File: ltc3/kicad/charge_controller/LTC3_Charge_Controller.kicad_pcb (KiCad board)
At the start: 4 copper layers, 85.2 x 81.3 mm, 119 parts, among them P1 MicroFit header, P2 MicroFit header, P3 S2BPHKS, P4 MicroFit header, P5 JST XH header, P7 JST XH header, Q1 ZVN4525E6, Q2 BSC028N06NS, Q3 BSC028N06NS, Q4 BSC028N06NS, Q5 BSC028N06NS, Q6 ZVP3310F, Q7 MMBT5550L, U1 PI2127, U2 PI2127, U3 LT8490, U4 LTC2990

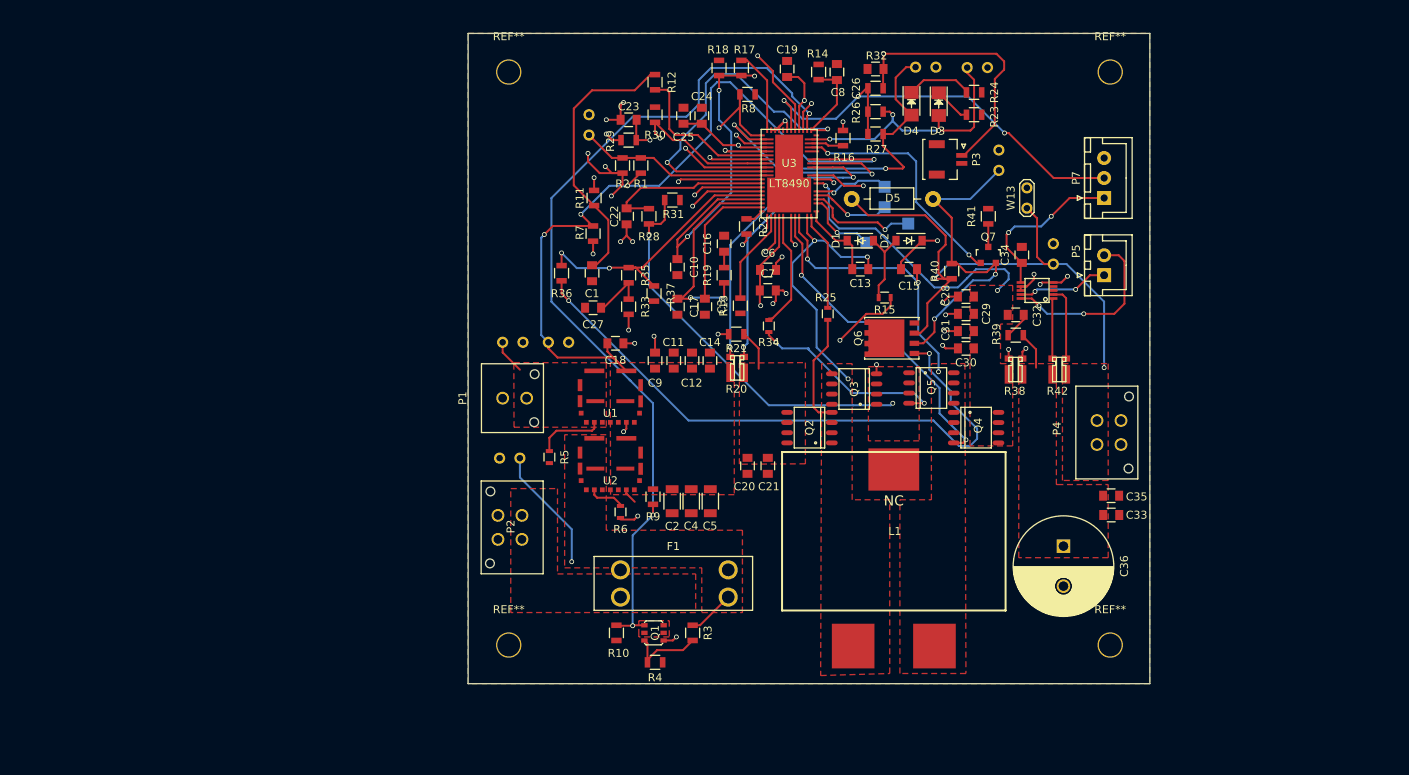
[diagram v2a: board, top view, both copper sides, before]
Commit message: LTC3: Update to charge controller schematic/PCB
-Adjusted resistors on charge controller for better current limiting
-Changed footprints of current sense resistors
-Began adjusting layout, making the board slightly larger
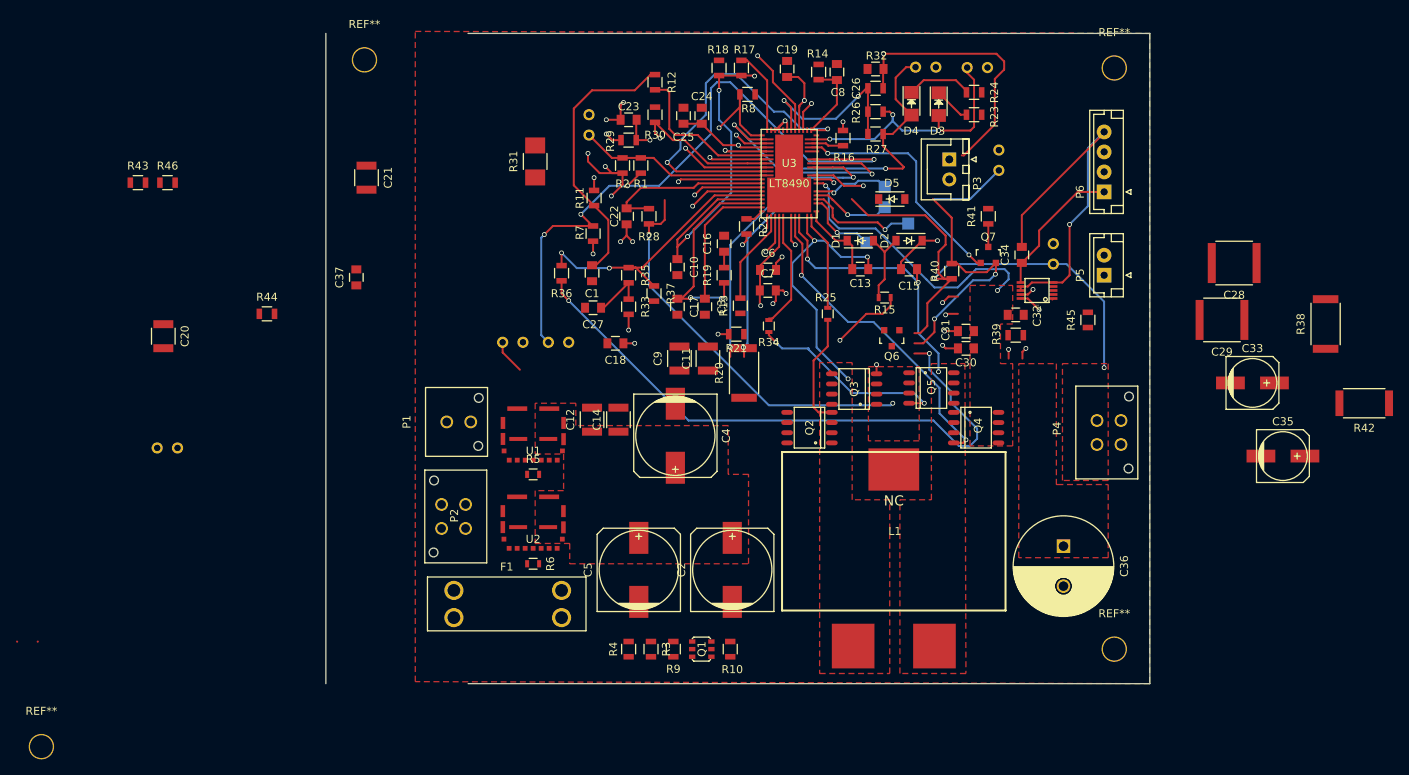
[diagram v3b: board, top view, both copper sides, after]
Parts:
- removed P7: JST XH header, Connectors_JST:JST_XH_B03B-XH-A_03x2.50mm_Straight
- removed the REF** at (104.1, 138.7)
- removed the REF** at (179.3, 138.7)
- removed the REF** at (179.3, 67.1)
- removed the REF** at (104.1, 67.1)
- removed W13: TEST, Measurement_Points:Test_Point_2Pads
- added C37: 0.1u, Capacitors_SMD:C_0805, F.Cu at (85.1, 92.7)
- added P6: CONN_01X04, Connectors_JST:JST_EH_B04B-EH-A_04x2.50mm_Straight, F.Cu at (178.6, 82.0)
- added R43: 75k, Resistors_SMD:R_0805, F.Cu at (57.8, 80.9)
- added R44: 12k, Resistors_SMD:R_0805, F.Cu at (73.9, 97.3)
- added R45: 75k, Resistors_SMD:R_0805, F.Cu at (176.5, 98.0)
- added R46: 12k, Resistors_SMD:R_0805, F.Cu at (61.5, 80.9)
- added REF**: MountingHole_0.1120in_#4, LTC3:MountingHole_0.1120in_number4, F.Cu at (179.8, 139.2)
- added REF**: MountingHole_0.1120in_#4, LTC3:MountingHole_0.1120in_number4, F.Cu at (45.7, 151.4)
- added REF**: MountingHole_0.1120in_#4, LTC3:MountingHole_0.1120in_number4, F.Cu at (86.1, 65.5)
- added REF**: MountingHole_0.1120in_#4, LTC3:MountingHole_0.1120in_number4, F.Cu at (179.8, 66.5)
- C1: value 0.33µ -> 0.33u
- C10, C8: value 10n -> 0.01u
- C11, C12, C14, C20, C21, C9: value 2.2µ -> 2.2u; footprint Capacitors_SMD:C_0805 -> Capacitors_SMD:C_1210
- C2, C4, C5: value 33µ -> 33u; footprint Capacitors_SMD:C_1206 -> Capacitors_SMD:c_elec_10x10
- C22, C23: value 1n -> 0.001u
- C24: value 4.7µ -> 4.7u
- C25: value 1µ -> 1u
- C26, C3, C31: value 100n -> 0.1u
- C27: value 0.18µ -> 0.18u
- C28, C29: value 4.7µ -> 4.7u; footprint Capacitors_SMD:C_0805 -> Capacitors_SMD:C_2220
- C30: value 1μ -> 1u
- C33, C35: value 10μ -> 10u; footprint Capacitors_SMD:C_0805 -> Capacitors_SMD:c_elec_6.3x7.7
- C34: value 0.1μ -> 0.1u
- C36: value 150μ -> 150u
- D5: value 1N4743A -> BZT52C13; footprint Choke_Axial_ThroughHole:Choke_Horizontal_RM10mm -> Diodes_SMD:SOD-123
- L1: value 10µH -> 10uH
- P3: value S2BPHKS -> JST XH header; footprint Connectors_JST:JST_SHL_SM02B-SHLS-TF_02x1.00mm_Angled -> Connectors_JST:JST_XH_B02B-XH-A_02x2.50mm_Straight
- P5: value JST XH header -> CONN_01X02; footprint Connectors_JST:JST_XH_B02B-XH-A_02x2.50mm_Straight -> Connectors_JST:JST_EH_B02B-EH-A_02x2.50mm_Straight
- Q6: footprint LTC3:PG-TDSON-8 -> TO_SOT_Packages_SMD:SOT-23
- R16: value 27.1k -> 25.5k
- R20, R38: value 5m -> 10m; footprint LTC3:CST0612 -> Resistors_SMD:R_2512
- R31: footprint Resistors_SMD:R_0805 -> Resistors_SMD:R_1210_HandSoldering
- R42: value 30m -> 100m; footprint LTC3:CST0612 -> Resistors_SMD:R_2512
- R5, R6: value 0 -> TBD
- moved C20 74.8 mm to (61.0, 100.1)
- moved C21 61.8 mm to (86.4, 80.3)
- moved W1 42.8 mm to (60.2, 114.0)
- moved R38 38.4 mm to (206.2, 98.6)
- moved R42 37.4 mm to (211.1, 108.5), turned to 180 degrees
- moved C28 33.8 mm to (194.8, 90.9)
- moved C29 32.0 mm to (193.3, 98.0)
- moved C33 24.2 mm to (197.1, 105.9)
- moved C35 22.0 mm to (200.9, 115.1)
- moved F1 21.0 mm to (103.9, 133.6)
- moved R9 19.2 mm to (124.7, 139.2)
- moved R31 17.8 mm to (107.4, 78.2), turned to 90 degrees
- moved C12 14.5 mm to (114.6, 110.5)
- moved R10 14.4 mm to (131.8, 139.2)
- moved C14 13.6 mm to (117.9, 110.5)
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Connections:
- net +3V3 renamed Net-(C24-Pad1)
- C20 pad 1: Net-(C20-Pad1) -> Net-(C18-Pad1)
- C21 pad 1: Net-(C20-Pad1) -> Net-(C18-Pad1)
- C34 pad 2: GND -> GNDREF
- P5 pad 1: /I2C_CLOCK -> Net-(D3-Pad2)
- P5 pad 2: /I2C_DATA -> GND
- Q1 pad 2: Net-(Q1-Pad1) -> (no net)
- Q1 pad 5: Net-(Q1-Pad1) -> (no net)
- Q1 pad 6: Net-(Q1-Pad1) -> (no net)
- Q2 pad 5: Net-(C20-Pad1) -> Net-(C18-Pad1)
- Q2 pad 6: Net-(C20-Pad1) -> Net-(C18-Pad1)
- Q2 pad 7: Net-(C20-Pad1) -> Net-(C18-Pad1)
- Q2 pad 8: Net-(C20-Pad1) -> Net-(C18-Pad1)
- Q4 pad 1: (no net) -> /SW2
- Q4 pad 2: (no net) -> /SW2
- R20 pad 1: Net-(C20-Pad1) -> Net-(C18-Pad1)
- R21 pad 1: Net-(C20-Pad1) -> Net-(R21-Pad1)
- R31 pad 1: Net-(Q3-Pad1) -> GND
- R31 pad 2: GND -> Net-(Q3-Pad1)
- U3 pad 41: Net-(R38-Pad3) -> Net-(C33-Pad1)
- U3 pad 42: Net-(R38-Pad4) -> /EXTVCC
- U3 pad 44: Net-(R20-Pad3) -> Net-(R21-Pad1)
- U3 pad 45: Net-(R20-Pad4) -> VIN
- U4 pad 1: Net-(R42-Pad4) -> Net-(R43-Pad2)
- U4 pad 2: Net-(R42-Pad3) -> Net-(R45-Pad2)
- U4 pad 5: GND -> GNDREF
- U4 pad 8: GND -> GNDREF
- U4 pad 9: GND -> GNDREF
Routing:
- net Net-(Q1-Pad1): track 110.4 -> 0.00 mm, vias 3 -> 0
- net VIN: track 98.5 -> 161.8 mm, vias 4 -> 8
- net GNDREF: track 0.00 -> 45.5 mm, vias 0 -> 1
- net Net-(R38-Pad3): track 44.5 -> 0.00 mm, vias 2 -> 0
- net Net-(R20-Pad4): track 43.5 -> 0.00 mm, vias 2 -> 0
- net Net-(R38-Pad4): track 42.0 -> 0.00 mm, vias 2 -> 0
- net /EXTVCC: track 35.6 -> 77.4 mm, vias 2 -> 4
- net Net-(C33-Pad1): track 4.72 -> 44.5 mm, vias 0 -> 2
- net Net-(R20-Pad3): track 37.0 -> 0.00 mm, vias 2 -> 0
- net Net-(C24-Pad1): track 97.3 -> 62.4 mm, vias 5 -> 4
- net Net-(F1-Pad2): track 21.5 -> 0.00 mm, vias 1 -> 0
- net GND: track 75.1 -> 54.8 mm, vias 26 -> 17
- net /I2C_CLOCK: track 11.4 -> 22.0 mm, vias 2 -> 1
- net /I2C_DATA: track 22.5 -> 32.7 mm, vias 2 -> 1
- net Net-(Q1-Pad3): track 9.86 -> 0.00 mm
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- removed copper zone on F.Cu, net Net-(C20-Pad1)
- removed copper zone on F.Cu, net Net-(F1-Pad1)
- removed copper zone on F.Cu, net Net-(F1-Pad2)
- removed copper zone on F.Cu, net Net-(P1-Pad2)
- removed copper zone on F.Cu, net Net-(Q1-Pad1)
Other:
- board size 85.2 x 81.3 mm -> 103 x 81.3 mm

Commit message: LTC3: Charge Controller Layout
Layout with via stapling and updated footprints.
It was quite an ordeal!
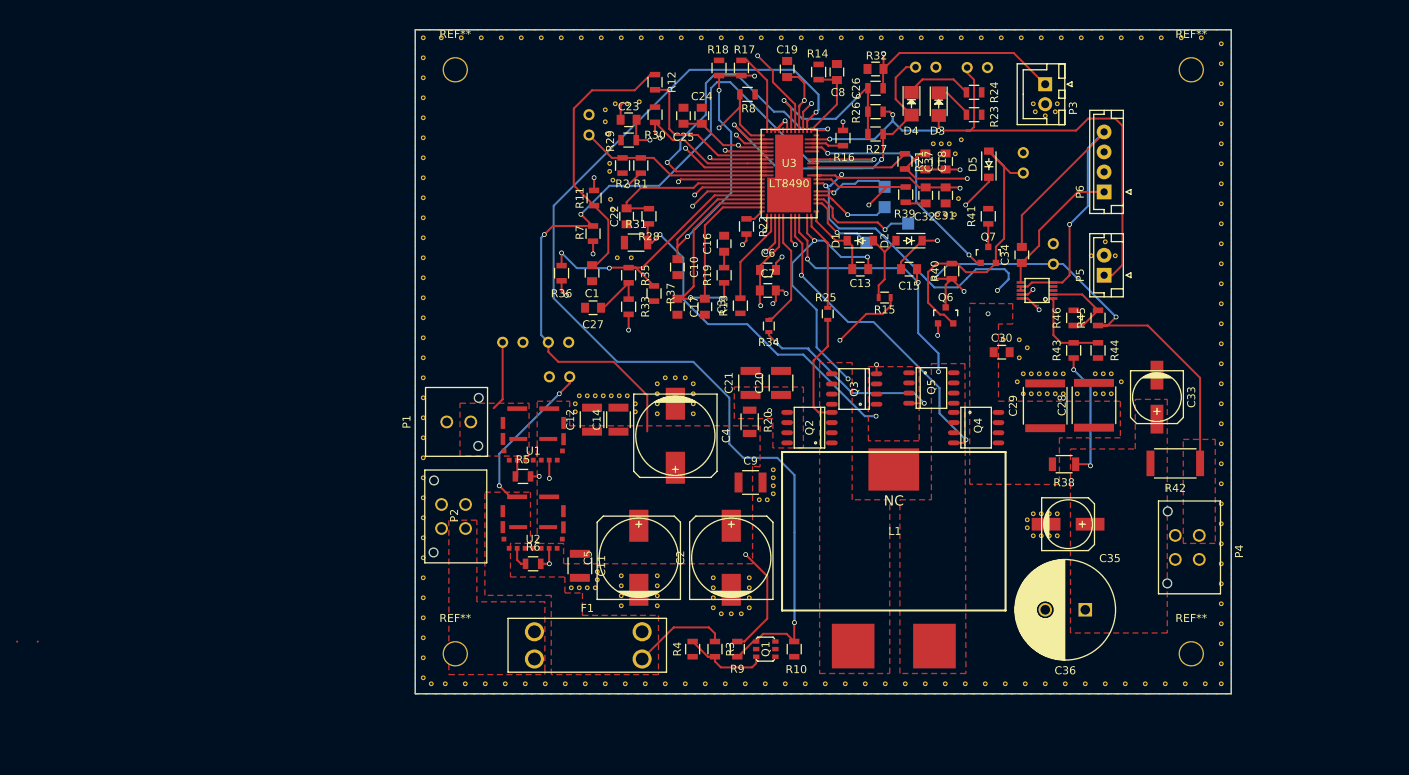
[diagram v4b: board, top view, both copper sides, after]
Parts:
- added REF**: Via_.6mm, LTC3:Via_.6mm, F.Cu at (116.9, 83.0)
- added REF**: Via_.6mm, LTC3:Via_.6mm, F.Cu at (157.2, 76.0)
- added REF**: Via_.6mm, LTC3:Via_.6mm, F.Cu at (122.7, 132.5)
- added REF**: Via_.6mm, LTC3:Via_.6mm, F.Cu at (122.7, 133.8)
- added REF**: Via_.6mm, LTC3:Via_.6mm, F.Cu at (118.2, 133.8)
- added REF**: Via_.6mm, LTC3:Via_.6mm, F.Cu at (118.2, 132.5)
- added REF**: Via_.6mm, LTC3:Via_.6mm, F.Cu at (118.2, 131.3)
- added REF**: Via_.6mm, LTC3:Via_.6mm, F.Cu at (118.2, 130.0)
- added REF**: Via_.6mm, LTC3:Via_.6mm, F.Cu at (122.7, 109.8)
- added REF**: Via_.6mm, LTC3:Via_.6mm, F.Cu at (122.7, 108.5)
- added REF**: Via_.6mm, LTC3:Via_.6mm, F.Cu at (122.7, 106.0)
- added REF**: Via_.6mm, LTC3:Via_.6mm, F.Cu at (123.7, 105.3)
- added REF**: Via_.6mm, LTC3:Via_.6mm, F.Cu at (158.2, 76.0)
- added REF**: Via_.6mm, LTC3:Via_.6mm, F.Cu at (125.0, 105.3)
- added REF**: Via_.6mm, LTC3:Via_.6mm, F.Cu at (126.2, 105.3)
- added REF**: Via_.6mm, LTC3:Via_.6mm, F.Cu at (127.2, 106.0)
- added REF**: Via_.6mm, LTC3:Via_.6mm, F.Cu at (127.2, 107.3)
- added REF**: Via_.6mm, LTC3:Via_.6mm, F.Cu at (127.2, 108.5)
- added REF**: Via_.6mm, LTC3:Via_.6mm, F.Cu at (127.2, 109.8)
- added REF**: Via_.6mm, LTC3:Via_.6mm, F.Cu at (119.5, 90.3)
- added REF**: Via_.6mm, LTC3:Via_.6mm, F.Cu at (117.7, 90.3)
- added REF**: Via_.6mm, LTC3:Via_.6mm, F.Cu at (117.2, 80.6)
- added REF**: Via_.6mm, LTC3:Via_.6mm, F.Cu at (116.8, 78.5)
- added REF**: Via_.6mm, LTC3:Via_.6mm, F.Cu at (159.2, 76.0)
- added REF**: Via_.6mm, LTC3:Via_.6mm, F.Cu at (116.8, 79.5)
- added REF**: Via_.6mm, LTC3:Via_.6mm, F.Cu at (116.5, 74.8)
- added REF**: Via_.6mm, LTC3:Via_.6mm, F.Cu at (116.2, 73.3)
- added REF**: Via_.6mm, LTC3:Via_.6mm, F.Cu at (116.2, 71.8)
- added REF**: Via_.6mm, LTC3:Via_.6mm, F.Cu at (117.5, 71.0)
- added REF**: Via_.6mm, LTC3:Via_.6mm, F.Cu at (119.0, 71.0)
- added REF**: Via_.6mm, LTC3:Via_.6mm, F.Cu at (120.5, 70.8)
- added REF**: Via_.6mm, LTC3:Via_.6mm, F.Cu at (94.5, 143.5)
- added REF**: Via_.6mm, LTC3:Via_.6mm, F.Cu at (96.2, 143.5)
- added REF**: Via_.6mm, LTC3:Via_.6mm, F.Cu at (98.7, 143.5)
- added REF**: Via_.6mm, LTC3:Via_.6mm, F.Cu at (160.7, 75.5)
- added REF**: Via_.6mm, LTC3:Via_.6mm, F.Cu at (101.2, 143.5)
- added REF**: Via_.6mm, LTC3:Via_.6mm, F.Cu at (103.7, 143.5)
- added REF**: Via_.6mm, LTC3:Via_.6mm, F.Cu at (106.2, 143.5)
- added REF**: Via_.6mm, LTC3:Via_.6mm, F.Cu at (108.7, 143.5)
- added REF**: Via_.6mm, LTC3:Via_.6mm, F.Cu at (111.2, 143.5)
- added REF**: Via_.6mm, LTC3:Via_.6mm, F.Cu at (113.7, 143.5)
- added REF**: Via_.6mm, LTC3:Via_.6mm, F.Cu at (116.2, 143.5)
- added REF**: Via_.6mm, LTC3:Via_.6mm, F.Cu at (118.7, 143.5)
- added REF**: Via_.6mm, LTC3:Via_.6mm, F.Cu at (121.2, 143.5)
- added REF**: Via_.6mm, LTC3:Via_.6mm, F.Cu at (123.7, 143.5)
- added REF**: Via_.6mm, LTC3:Via_.6mm, F.Cu at (160.0, 77.3)
- added REF**: Via_.6mm, LTC3:Via_.6mm, F.Cu at (126.2, 143.5)
- added REF**: Via_.6mm, LTC3:Via_.6mm, F.Cu at (128.7, 143.5)
- added REF**: Via_.6mm, LTC3:Via_.6mm, F.Cu at (131.2, 143.5)
- added REF**: Via_.6mm, LTC3:Via_.6mm, F.Cu at (133.7, 143.5)
- added REF**: Via_.6mm, LTC3:Via_.6mm, F.Cu at (136.2, 143.5)
- added REF**: Via_.6mm, LTC3:Via_.6mm, F.Cu at (138.7, 143.5)
- added REF**: Via_.6mm, LTC3:Via_.6mm, F.Cu at (141.2, 143.5)
- added REF**: Via_.6mm, LTC3:Via_.6mm, F.Cu at (143.7, 143.5)
- added REF**: Via_.6mm, LTC3:Via_.6mm, F.Cu at (146.2, 143.5)
- added REF**: Via_.6mm, LTC3:Via_.6mm, F.Cu at (93.5, 142.8)
- added REF**: Via_.6mm, LTC3:Via_.6mm, F.Cu at (160.4, 82.9)
- added REF**: Via_.6mm, LTC3:Via_.6mm, F.Cu at (93.5, 140.3)
- added REF**: Via_.6mm, LTC3:Via_.6mm, F.Cu at (93.5, 137.8)
- added REF**: Via_.6mm, LTC3:Via_.6mm, F.Cu at (93.5, 135.3)
- added REF**: Via_.6mm, LTC3:Via_.6mm, F.Cu at (93.5, 132.8)
- added REF**: Via_.6mm, LTC3:Via_.6mm, F.Cu at (93.5, 130.3)
- added REF**: Via_.6mm, LTC3:Via_.6mm, F.Cu at (93.5, 127.8)
- added REF**: Via_.6mm, LTC3:Via_.6mm, F.Cu at (93.5, 125.3)
- added REF**: Via_.6mm, LTC3:Via_.6mm, F.Cu at (93.5, 122.8)
- added REF**: Via_.6mm, LTC3:Via_.6mm, F.Cu at (93.5, 120.3)
- added REF**: Via_.6mm, LTC3:Via_.6mm, F.Cu at (93.5, 117.8)
- added REF**: Via_.6mm, LTC3:Via_.6mm, F.Cu at (159.9, 84.9)
- added REF**: Via_.6mm, LTC3:Via_.6mm, F.Cu at (93.5, 115.3)
- added REF**: Via_.6mm, LTC3:Via_.6mm, F.Cu at (93.5, 112.8)
- added REF**: Via_.6mm, LTC3:Via_.6mm, F.Cu at (93.5, 110.3)
- added REF**: Via_.6mm, LTC3:Via_.6mm, F.Cu at (93.5, 107.8)
- added REF**: Via_.6mm, LTC3:Via_.6mm, F.Cu at (93.5, 105.3)
- added REF**: Via_.6mm, LTC3:Via_.6mm, F.Cu at (93.5, 102.8)
- added REF**: Via_.6mm, LTC3:Via_.6mm, F.Cu at (93.5, 100.3)
- added REF**: Via_.6mm, LTC3:Via_.6mm, F.Cu at (93.5, 97.8)
- added REF**: Via_.6mm, LTC3:Via_.6mm, F.Cu at (93.5, 95.3)
- added REF**: Via_.6mm, LTC3:Via_.6mm, F.Cu at (93.5, 92.8)
- added REF**: Via_.6mm, LTC3:Via_.6mm, F.Cu at (158.8, 84.9)
- added REF**: Via_.6mm, LTC3:Via_.6mm, F.Cu at (93.5, 90.3)
- added REF**: Via_.6mm, LTC3:Via_.6mm, F.Cu at (93.5, 87.8)
- added REF**: Via_.6mm, LTC3:Via_.6mm, F.Cu at (93.5, 85.3)
- added REF**: Via_.6mm, LTC3:Via_.6mm, F.Cu at (93.5, 82.8)
- added REF**: Via_.6mm, LTC3:Via_.6mm, F.Cu at (93.5, 80.3)
- added REF**: Via_.6mm, LTC3:Via_.6mm, F.Cu at (93.5, 77.8)
- added REF**: Via_.6mm, LTC3:Via_.6mm, F.Cu at (93.5, 75.3)
- added REF**: Via_.6mm, LTC3:Via_.6mm, F.Cu at (93.5, 72.8)
- added REF**: Via_.6mm, LTC3:Via_.6mm, F.Cu at (93.5, 70.3)
- added REF**: Via_.6mm, LTC3:Via_.6mm, F.Cu at (93.5, 67.8)
- added REF**: Via_.6mm, LTC3:Via_.6mm, F.Cu at (157.8, 84.9)
- added REF**: Via_.6mm, LTC3:Via_.6mm, F.Cu at (93.5, 65.3)
- added REF**: Via_.6mm, LTC3:Via_.6mm, F.Cu at (93.5, 62.8)
- added REF**: Via_.6mm, LTC3:Via_.6mm, F.Cu at (95.7, 62.8)
- added REF**: Via_.6mm, LTC3:Via_.6mm, F.Cu at (98.2, 62.8)
- added REF**: Via_.6mm, LTC3:Via_.6mm, F.Cu at (100.7, 62.8)
- added REF**: Via_.6mm, LTC3:Via_.6mm, F.Cu at (103.2, 62.8)
- added REF**: Via_.6mm, LTC3:Via_.6mm, F.Cu at (105.7, 62.8)
- added REF**: Via_.6mm, LTC3:Via_.6mm, F.Cu at (108.2, 62.8)
- added REF**: Via_.6mm, LTC3:Via_.6mm, F.Cu at (110.7, 62.8)
- added REF**: Via_.6mm, LTC3:Via_.6mm, F.Cu at (113.2, 62.8)
- added REF**: Via_.6mm, LTC3:Via_.6mm, F.Cu at (177.0, 90.0)
- added REF**: Via_.6mm, LTC3:Via_.6mm, F.Cu at (115.7, 62.8)
- added REF**: Via_.6mm, LTC3:Via_.6mm, F.Cu at (118.2, 62.8)
- added REF**: Via_.6mm, LTC3:Via_.6mm, F.Cu at (120.7, 62.8)
- added REF**: Via_.6mm, LTC3:Via_.6mm, F.Cu at (123.2, 62.8)
- added REF**: Via_.6mm, LTC3:Via_.6mm, F.Cu at (125.7, 62.8)
- added REF**: Via_.6mm, LTC3:Via_.6mm, F.Cu at (128.2, 62.8)
- added REF**: Via_.6mm, LTC3:Via_.6mm, F.Cu at (130.7, 62.8)
- added REF**: Via_.6mm, LTC3:Via_.6mm, F.Cu at (133.2, 62.8)
- added REF**: Via_.6mm, LTC3:Via_.6mm, F.Cu at (135.7, 62.8)
- added REF**: Via_.6mm, LTC3:Via_.6mm, F.Cu at (138.2, 62.8)
- added REF**: Via_.6mm, LTC3:Via_.6mm, F.Cu at (117.2, 84.3)
- added REF**: Via_.6mm, LTC3:Via_.6mm, F.Cu at (178.7, 88.3)
- added REF**: Via_.6mm, LTC3:Via_.6mm, F.Cu at (140.7, 62.8)
- added REF**: Via_.6mm, LTC3:Via_.6mm, F.Cu at (143.2, 62.8)
- added REF**: Via_.6mm, LTC3:Via_.6mm, F.Cu at (145.7, 62.8)
- added REF**: Via_.6mm, LTC3:Via_.6mm, F.Cu at (148.2, 62.8)
- added REF**: Via_.6mm, LTC3:Via_.6mm, F.Cu at (150.7, 62.8)
- added REF**: Via_.6mm, LTC3:Via_.6mm, F.Cu at (153.2, 62.8)
- added REF**: Via_.6mm, LTC3:Via_.6mm, F.Cu at (155.7, 62.8)
- added REF**: Via_.6mm, LTC3:Via_.6mm, F.Cu at (158.2, 62.8)
- added REF**: Via_.6mm, LTC3:Via_.6mm, F.Cu at (160.7, 62.8)
- added REF**: Via_.6mm, LTC3:Via_.6mm, F.Cu at (163.2, 62.8)
- added REF**: Via_.6mm, LTC3:Via_.6mm, F.Cu at (180.0, 90.0)
- added REF**: Via_.6mm, LTC3:Via_.6mm, F.Cu at (165.7, 62.8)
- added REF**: Via_.6mm, LTC3:Via_.6mm, F.Cu at (168.2, 62.8)
- added REF**: Via_.6mm, LTC3:Via_.6mm, F.Cu at (170.7, 62.8)
- added REF**: Via_.6mm, LTC3:Via_.6mm, F.Cu at (173.2, 62.8)
- added REF**: Via_.6mm, LTC3:Via_.6mm, F.Cu at (175.7, 62.8)
- added REF**: Via_.6mm, LTC3:Via_.6mm, F.Cu at (178.2, 62.8)
- added REF**: Via_.6mm, LTC3:Via_.6mm, F.Cu at (180.7, 62.8)
- added REF**: Via_.6mm, LTC3:Via_.6mm, F.Cu at (183.2, 62.8)
- added REF**: Via_.6mm, LTC3:Via_.6mm, F.Cu at (185.7, 62.8)
- added REF**: Via_.6mm, LTC3:Via_.6mm, F.Cu at (188.2, 62.8)
- added REF**: Via_.6mm, LTC3:Via_.6mm, F.Cu at (170.0, 72.0)
- added REF**: Via_.6mm, LTC3:Via_.6mm, F.Cu at (190.7, 62.8)
- added REF**: Via_.6mm, LTC3:Via_.6mm, F.Cu at (193.2, 63.5)
- added REF**: Via_.6mm, LTC3:Via_.6mm, F.Cu at (193.2, 66.0)
- added REF**: Via_.6mm, LTC3:Via_.6mm, F.Cu at (193.2, 68.5)
- added REF**: Via_.6mm, LTC3:Via_.6mm, F.Cu at (193.2, 71.0)
- added REF**: Via_.6mm, LTC3:Via_.6mm, F.Cu at (193.2, 73.5)
- added REF**: Via_.6mm, LTC3:Via_.6mm, F.Cu at (193.2, 76.0)
- added REF**: Via_.6mm, LTC3:Via_.6mm, F.Cu at (193.2, 78.5)
- added REF**: Via_.6mm, LTC3:Via_.6mm, F.Cu at (193.2, 81.0)
- added REF**: Via_.6mm, LTC3:Via_.6mm, F.Cu at (193.2, 83.5)
- added REF**: Via_.6mm, LTC3:Via_.6mm, F.Cu at (172.5, 72.0)
- added REF**: Via_.6mm, LTC3:Via_.6mm, F.Cu at (193.2, 86.0)
- added REF**: Via_.6mm, LTC3:Via_.6mm, F.Cu at (193.2, 88.5)
- added REF**: Via_.6mm, LTC3:Via_.6mm, F.Cu at (193.2, 91.0)
- added REF**: Via_.6mm, LTC3:Via_.6mm, F.Cu at (193.2, 93.5)
- added REF**: Via_.6mm, LTC3:Via_.6mm, F.Cu at (193.2, 96.0)
- added REF**: Via_.6mm, LTC3:Via_.6mm, F.Cu at (193.2, 98.5)
- added REF**: Via_.6mm, LTC3:Via_.6mm, F.Cu at (193.2, 101.0)
- added REF**: Via_.6mm, LTC3:Via_.6mm, F.Cu at (193.2, 103.5)
- added REF**: Via_.6mm, LTC3:Via_.6mm, F.Cu at (193.2, 106.0)
- added REF**: Via_.6mm, LTC3:Via_.6mm, F.Cu at (193.2, 108.5)
- added REF**: Via_.6mm, LTC3:Via_.6mm, F.Cu at (171.2, 72.5)
- added REF**: Via_.6mm, LTC3:Via_.6mm, F.Cu at (193.2, 111.0)
- added REF**: Via_.6mm, LTC3:Via_.6mm, F.Cu at (193.2, 113.5)
- added REF**: Via_.6mm, LTC3:Via_.6mm, F.Cu at (193.2, 116.0)
- added REF**: Via_.6mm, LTC3:Via_.6mm, F.Cu at (193.2, 118.5)
- added REF**: Via_.6mm, LTC3:Via_.6mm, F.Cu at (193.2, 121.0)
- added REF**: Via_.6mm, LTC3:Via_.6mm, F.Cu at (193.2, 123.5)
- added REF**: Via_.6mm, LTC3:Via_.6mm, F.Cu at (193.2, 126.0)
- added REF**: Via_.6mm, LTC3:Via_.6mm, F.Cu at (193.2, 128.5)
- added REF**: Via_.6mm, LTC3:Via_.6mm, F.Cu at (193.2, 131.0)
- added REF**: Via_.6mm, LTC3:Via_.6mm, F.Cu at (193.2, 133.5)
- added REF**: Via_.6mm, LTC3:Via_.6mm, F.Cu at (169.7, 71.0)
- added REF**: Via_.6mm, LTC3:Via_.6mm, F.Cu at (193.2, 136.0)
- added REF**: Via_.6mm, LTC3:Via_.6mm, F.Cu at (193.2, 138.5)
- added REF**: Via_.6mm, LTC3:Via_.6mm, F.Cu at (193.2, 141.0)
- added REF**: Via_.6mm, LTC3:Via_.6mm, F.Cu at (193.2, 143.5)
- added REF**: Via_.6mm, LTC3:Via_.6mm, F.Cu at (191.2, 143.5)
- added REF**: Via_.6mm, LTC3:Via_.6mm, F.Cu at (188.7, 143.5)
- added REF**: Via_.6mm, LTC3:Via_.6mm, F.Cu at (186.2, 143.5)
- added REF**: Via_.6mm, LTC3:Via_.6mm, F.Cu at (183.7, 143.5)
- added REF**: Via_.6mm, LTC3:Via_.6mm, F.Cu at (181.2, 143.5)
- added REF**: Via_.6mm, LTC3:Via_.6mm, F.Cu at (178.7, 143.5)
- added REF**: Via_.6mm, LTC3:Via_.6mm, F.Cu at (172.7, 71.0)
- added REF**: Via_.6mm, LTC3:Via_.6mm, F.Cu at (176.2, 143.5)
- added REF**: Via_.6mm, LTC3:Via_.6mm, F.Cu at (173.7, 143.5)
- added REF**: Via_.6mm, LTC3:Via_.6mm, F.Cu at (171.2, 143.5)
- added REF**: Via_.6mm, LTC3:Via_.6mm, F.Cu at (168.7, 143.5)
- added REF**: Via_.6mm, LTC3:Via_.6mm, F.Cu at (166.2, 143.5)
- added REF**: Via_.6mm, LTC3:Via_.6mm, F.Cu at (163.7, 143.5)
- added REF**: Via_.6mm, LTC3:Via_.6mm, F.Cu at (158.7, 143.5)
- added REF**: Via_.6mm, LTC3:Via_.6mm, F.Cu at (161.2, 143.5)
- added REF**: Via_.6mm, LTC3:Via_.6mm, F.Cu at (156.2, 143.5)
- added REF**: Via_.6mm, LTC3:Via_.6mm, F.Cu at (153.7, 143.5)
- added REF**: Via_.6mm, LTC3:Via_.6mm, F.Cu at (169.0, 101.5)
- added REF**: Via_.6mm, LTC3:Via_.6mm, F.Cu at (151.2, 143.5)
- added REF**: Via_.6mm, LTC3:Via_.6mm, F.Cu at (148.7, 143.5)
- added REF**: Via_.6mm, LTC3:Via_.6mm, F.Cu at (168.0, 100.5)
- added REF**: Via_.6mm, LTC3:Via_.6mm, F.Cu at (168.0, 102.8)
- added REF**: Via_.6mm, LTC3:Via_.6mm, F.Cu at (122.7, 107.3)
- added REF**: Via_.6mm, LTC3:Via_.6mm, F.Cu at (166.0, 100.5)
- added REF**: Via_.6mm, LTC3:Via_.6mm, F.Cu at (167.7, 105.8)
- added REF**: Via_.6mm, LTC3:Via_.6mm, F.Cu at (180.7, 105.8)
- added REF**: Via_.6mm, LTC3:Via_.6mm, F.Cu at (179.5, 104.8)
- added REF**: Via_.6mm, LTC3:Via_.6mm, F.Cu at (178.5, 104.8)
- added REF**: Via_.6mm, LTC3:Via_.6mm, F.Cu at (177.5, 104.8)
- added REF**: Via_.6mm, LTC3:Via_.6mm, F.Cu at (173.5, 104.8)
- added REF**: Via_.6mm, LTC3:Via_.6mm, F.Cu at (172.5, 104.8)
- added REF**: Via_.6mm, LTC3:Via_.6mm, F.Cu at (171.5, 104.8)
- added REF**: Via_.6mm, LTC3:Via_.6mm, F.Cu at (170.5, 104.8)
- added REF**: Via_.6mm, LTC3:Via_.6mm, F.Cu at (115.0, 131.5)
- added REF**: Via_.6mm, LTC3:Via_.6mm, F.Cu at (169.5, 104.8)
- added REF**: Via_.6mm, LTC3:Via_.6mm, F.Cu at (168.5, 104.8)
- added REF**: Via_.6mm, LTC3:Via_.6mm, F.Cu at (168.5, 107.3)
- added REF**: Via_.6mm, LTC3:Via_.6mm, F.Cu at (169.5, 107.3)
- added REF**: Via_.6mm, LTC3:Via_.6mm, F.Cu at (170.5, 107.3)
- added REF**: Via_.6mm, LTC3:Via_.6mm, F.Cu at (171.5, 107.3)
- added REF**: Via_.6mm, LTC3:Via_.6mm, F.Cu at (172.5, 107.3)
- added REF**: Via_.6mm, LTC3:Via_.6mm, F.Cu at (173.5, 107.3)
- added REF**: Via_.6mm, LTC3:Via_.6mm, F.Cu at (175.2, 107.3)
- added REF**: Via_.6mm, LTC3:Via_.6mm, F.Cu at (177.5, 107.3)
- added REF**: Via_.6mm, LTC3:Via_.6mm, F.Cu at (112.0, 131.5)
- added REF**: Via_.6mm, LTC3:Via_.6mm, F.Cu at (178.5, 107.3)
- added REF**: Via_.6mm, LTC3:Via_.6mm, F.Cu at (179.5, 107.3)
- added REF**: Via_.6mm, LTC3:Via_.6mm, F.Cu at (170.0, 133.0)
- added REF**: Via_.6mm, LTC3:Via_.6mm, F.Cu at (172.5, 133.0)
- added REF**: Via_.6mm, LTC3:Via_.6mm, F.Cu at (172.5, 135.5)
- added REF**: Via_.6mm, LTC3:Via_.6mm, F.Cu at (170.0, 135.5)
- added REF**: Via_.6mm, LTC3:Via_.6mm, F.Cu at (171.2, 136.0)
- added REF**: Via_.6mm, LTC3:Via_.6mm, F.Cu at (171.2, 132.8)
- added REF**: Via_.6mm, LTC3:Via_.6mm, F.Cu at (169.7, 134.3)
- added REF**: Via_.6mm, LTC3:Via_.6mm, F.Cu at (172.7, 134.3)
- added REF**: Via_.6mm, LTC3:Via_.6mm, F.Cu at (115.2, 129.5)
- added REF**: Via_.6mm, LTC3:Via_.6mm, F.Cu at (172.7, 125.0)
- added REF**: Via_.6mm, LTC3:Via_.6mm, F.Cu at (171.7, 125.0)
- added REF**: Via_.6mm, LTC3:Via_.6mm, F.Cu at (170.7, 125.0)
- added REF**: Via_.6mm, LTC3:Via_.6mm, F.Cu at (169.7, 125.0)
- added REF**: Via_.6mm, LTC3:Via_.6mm, F.Cu at (169.0, 124.0)
- added REF**: Via_.6mm, LTC3:Via_.6mm, F.Cu at (169.0, 123.0)
- added REF**: Via_.6mm, LTC3:Via_.6mm, F.Cu at (169.7, 122.3)
- added REF**: Via_.6mm, LTC3:Via_.6mm, F.Cu at (170.7, 122.3)
- added REF**: Via_.6mm, LTC3:Via_.6mm, F.Cu at (171.7, 122.3)
- added REF**: Via_.6mm, LTC3:Via_.6mm, F.Cu at (172.7, 122.3)
- added REF**: Via_.6mm, LTC3:Via_.6mm, F.Cu at (113.0, 131.5)
- added REF**: Via_.6mm, LTC3:Via_.6mm, F.Cu at (135.5, 120.5)
- added REF**: Via_.6mm, LTC3:Via_.6mm, F.Cu at (136.5, 120.5)
- added REF**: Via_.6mm, LTC3:Via_.6mm, F.Cu at (137.2, 116.8)
- added REF**: Via_.6mm, LTC3:Via_.6mm, F.Cu at (137.2, 119.8)
- added REF**: Via_.6mm, LTC3:Via_.6mm, F.Cu at (137.2, 118.8)
- added REF**: Via_.6mm, LTC3:Via_.6mm, F.Cu at (137.2, 117.8)
- added REF**: Via_.6mm, LTC3:Via_.6mm, F.Cu at (112.5, 109.5)
- added REF**: Via_.6mm, LTC3:Via_.6mm, F.Cu at (112.5, 108.5)
- added REF**: Via_.6mm, LTC3:Via_.6mm, F.Cu at (113.0, 107.5)
- added REF**: Via_.6mm, LTC3:Via_.6mm, F.Cu at (114.0, 107.5)
- added REF**: Via_.6mm, LTC3:Via_.6mm, F.Cu at (114.0, 131.5)
- added REF**: Via_.6mm, LTC3:Via_.6mm, F.Cu at (115.0, 107.5)
- added REF**: Via_.6mm, LTC3:Via_.6mm, F.Cu at (116.0, 107.5)
- added REF**: Via_.6mm, LTC3:Via_.6mm, F.Cu at (117.0, 107.5)
- added REF**: Via_.6mm, LTC3:Via_.6mm, F.Cu at (118.0, 107.5)
- added REF**: Via_.6mm, LTC3:Via_.6mm, F.Cu at (119.0, 107.5)
- added REF**: Via_.6mm, LTC3:Via_.6mm, F.Cu at (120.0, 108.5)
- added REF**: Via_.6mm, LTC3:Via_.6mm, F.Cu at (120.0, 109.5)
- added REF**: Via_.6mm, LTC3:Via_.6mm, F.Cu at (134.2, 130.3)
- added REF**: Via_.6mm, LTC3:Via_.6mm, F.Cu at (134.2, 131.5)
- added REF**: Via_.6mm, LTC3:Via_.6mm, F.Cu at (134.2, 132.8)
- added REF**: Via_.6mm, LTC3:Via_.6mm, F.Cu at (115.2, 130.5)
- added REF**: Via_.6mm, LTC3:Via_.6mm, F.Cu at (134.2, 134.0)
- added REF**: Via_.6mm, LTC3:Via_.6mm, F.Cu at (133.2, 134.8)
- added REF**: Via_.6mm, LTC3:Via_.6mm, F.Cu at (132.0, 134.8)
- added REF**: Via_.6mm, LTC3:Via_.6mm, F.Cu at (130.7, 134.8)
- added REF**: Via_.6mm, LTC3:Via_.6mm, F.Cu at (129.7, 134.0)
- added REF**: Via_.6mm, LTC3:Via_.6mm, F.Cu at (129.7, 132.8)
- added REF**: Via_.6mm, LTC3:Via_.6mm, F.Cu at (129.7, 131.5)
- added REF**: Via_.6mm, LTC3:Via_.6mm, F.Cu at (129.7, 130.3)
- added REF**: Via_.6mm, LTC3:Via_.6mm, F.Cu at (122.7, 130.0)
- added REF**: Via_.6mm, LTC3:Via_.6mm, F.Cu at (122.7, 131.3)
- P5: value CONN_01X02 -> JST XH header
- P6: value CONN_01X04 -> JST XH header
- R20, R38: footprint Resistors_SMD:R_2512 -> Resistors_SMD:R_1206
- R31: footprint Resistors_SMD:R_1210_HandSoldering -> Resistors_SMD:R_1206
- R42: value 100m -> 60m
- R5, R6: value TBD -> 0; footprint Resistors_SMD:R_0603 -> Resistors_SMD:R_0805
- moved R43 118.8 mm to (174.8, 101.9), turned to 90 degrees
- moved R46 114.5 mm to (174.8, 97.8), turned to 90 degrees
- moved R44 104.0 mm to (177.8, 101.9), turned to 270 degrees
- moved C20 77.4 mm to (138.2, 105.9), turned to 90 degrees
- moved C37 75.1 mm to (158.8, 78.2)
- moved C21 54.4 mm to (134.4, 105.9), turned to 90 degrees
- moved REF** 53.0 mm to (97.5, 139.8)
- moved W1 49.8 mm to (109.2, 105.2)
- moved C18 44.9 mm to (156.2, 78.2), turned to 270 degrees
- moved R38 37.1 mm to (173.6, 116.1), turned to 180 degrees
- moved C11 30.5 mm to (113.0, 128.8), turned to 270 degrees
- moved R21 30.2 mm to (153.7, 78.2), turned to 270 degrees
- moved C35 28.2 mm to (174.1, 123.6)
- moved C28 25.0 mm to (177.3, 108.7), turned to 90 degrees
- moved R42 24.8 mm to (187.5, 116.0)
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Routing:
- net Net-(Q1-Pad1): track 0.00 -> 130.4 mm, vias 0 -> 2
- net Net-(C18-Pad1): track 15.0 -> 88.6 mm
- net Net-(D3-Pad2): track 35.3 -> 76.9 mm
- net Net-(F1-Pad2): track 0.00 -> 32.6 mm, vias 0 -> 2
- net Net-(C33-Pad1): track 44.5 -> 72.0 mm, vias 2 -> 3
- net VIN: track 161.8 -> 139.6 mm, vias 8 -> 6
- net Net-(Q6-Pad1): track 76.8 -> 56.3 mm
- net GND: track 54.8 -> 38.8 mm, vias 17 -> 10
- net /VBATT: track 64.6 -> 79.4 mm, vias 2 -> 4
- net Net-(Q1-Pad3): track 0.00 -> 10.7 mm
- net Net-(R43-Pad2): track 0.20 -> 10.8 mm
- net Net-(R45-Pad2): track 0.01 -> 10.2 mm
- net Net-(R21-Pad1): track 2.51 -> 12.2 mm
- net Net-(C26-Pad1): track 65.2 -> 58.3 mm
- net Net-(Q3-Pad1): track 49.1 -> 44.2 mm
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- added copper zone on B.Cu, net GND
- added copper zone on In2.Cu, net GND
- added copper zone on F.Cu, net Net-(C18-Pad1)
- added copper zone on F.Cu, net Net-(F1-Pad1)
- added copper zone on F.Cu, net Net-(F1-Pad2)
- added copper zone on F.Cu, net Net-(P1-Pad2)
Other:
- board size 103 x 81.3 mm -> 102 x 83 mm
- board text removed: "Remove thermals for all power planes"
